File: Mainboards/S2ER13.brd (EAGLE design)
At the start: 43 x 72 mm, 52 parts, among them IC1 LD1117S33, IC2 CC1101RTK, IC3 STM32F051C8, Q1 IRLML9301, Q2 8M, X1 VCC, X2 CLK, X3 GND, X4 DIO, X5 RST, X6 NC

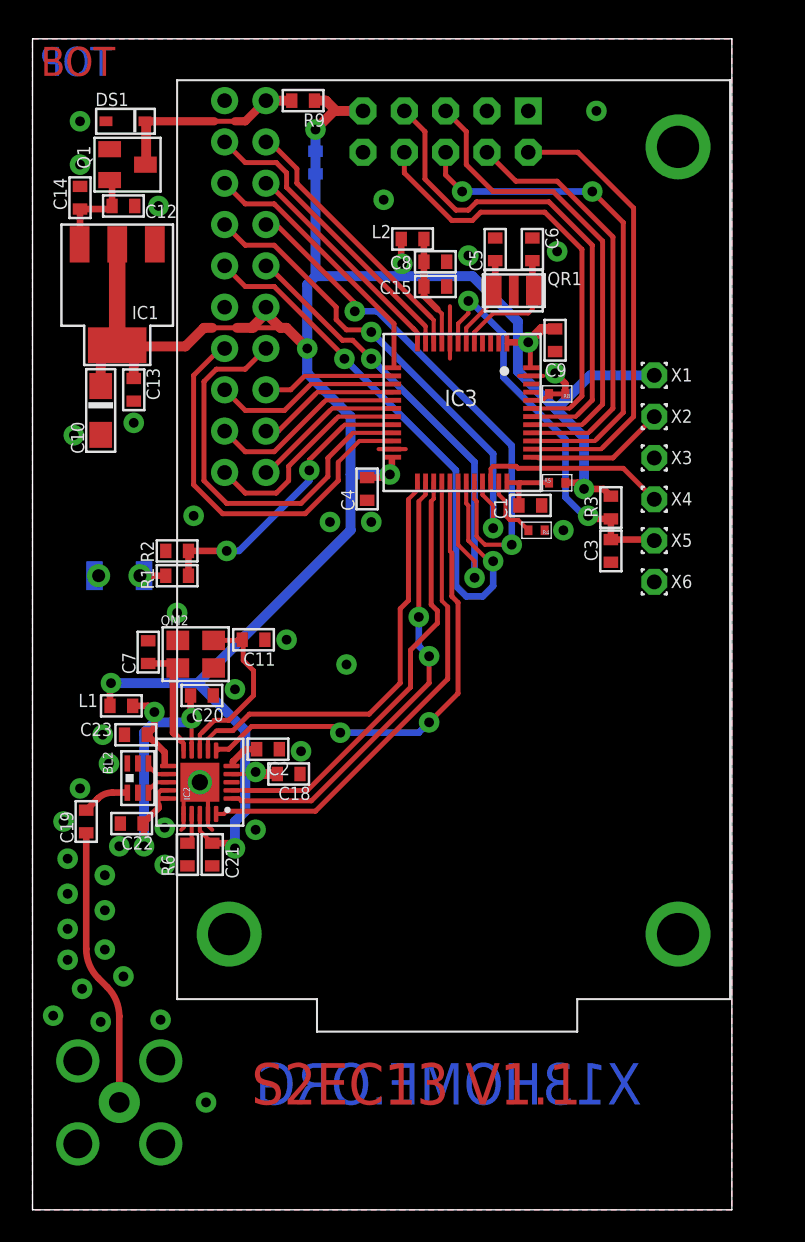
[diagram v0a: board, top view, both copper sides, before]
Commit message: Added prototypes
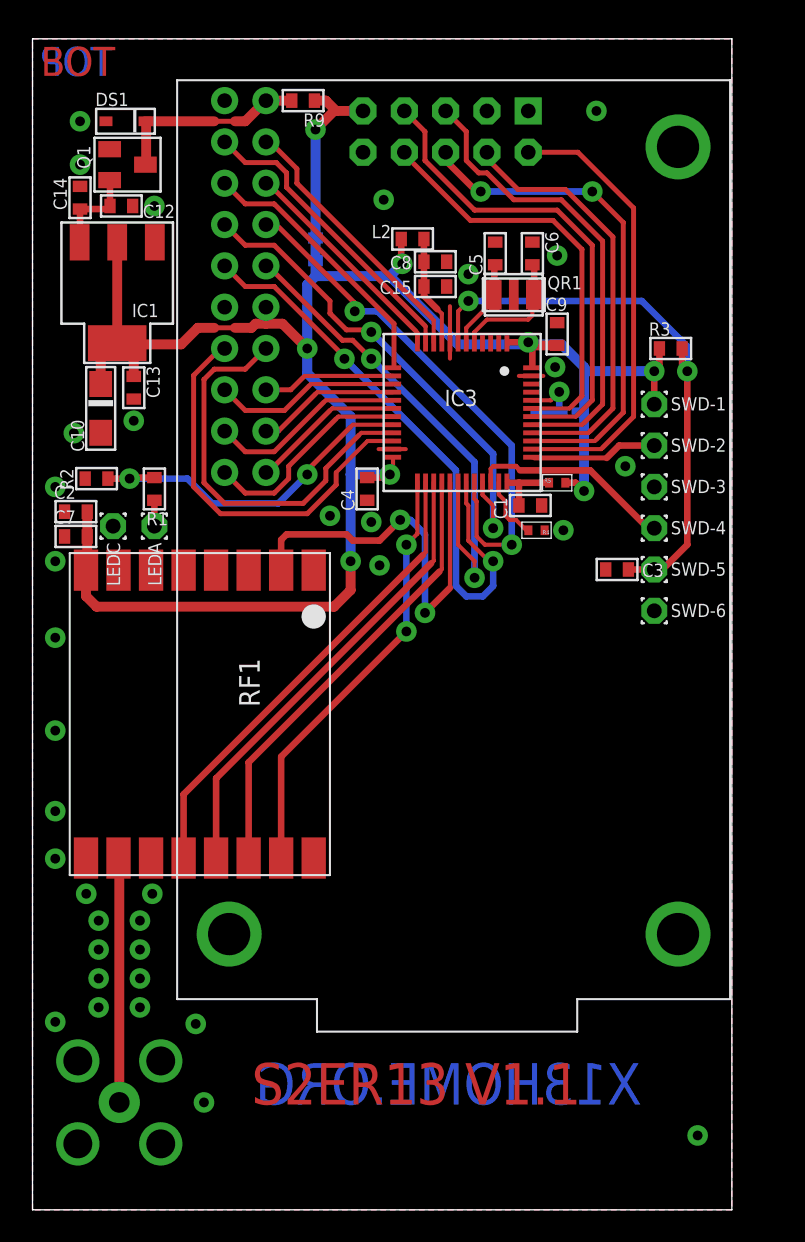
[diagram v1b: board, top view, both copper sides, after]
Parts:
- removed ANT: SMA-BU, Conn:BU-SMA-V
- removed BL2: 0896BM15A0001, RF:BL
- removed C11: 22p, RCL:0603
- removed C18, C20, C21, C22, C23: 100n, RCL:0603
- removed C19: 100p, RCL:0603
- removed IC2: CC1101RTK, RF:VQFN20
- removed L1: 10uH, RCL:0603
- removed LED1: OPT, Optic:T1-3/4
- removed LED2: OPT, Optic:1206
- removed QM2: 26M, QUARTZ:SMD_4P_3.2X2.5
- removed R6: 56k, RCL:0603
- removed R8: 0R, RCL:0402
- removed X1: VCC, Conn:T1.6/0.9
- removed X2: CLK, Conn:T1.6/0.9
- removed X4: DIO, Conn:T1.6/0.9
- removed X5: RST, Conn:T1.6/0.9
- removed X6: NC, Conn:T1.6/0.9
- added BR1: BR, Conn:BR
- added LEDA: LEDA, Conn:T1.6/0.9
- added LEDC, SWD-3: GND, Conn:T1.6/0.9
- added RF1: RFM69W, RF:RFM69
- added SWD-1: VCC, Conn:T1.6/0.9
- added SWD-2: CLK, Conn:T1.6/0.9
- added SWD-4: DIO, Conn:T1.6/0.9
- added SWD-5: /RST, Conn:T1.6/0.9
- added SWD-6: NC, Conn:T1.6/0.9
- C2: value 100n -> 1u
- C7: value 22p -> 100n
- X3: value GND -> SMA-BU; device Conn:T1.6/0.9 -> Conn:BU-SMA-V
- moved X3 51.5 mm to (5.33, 6.60), flipped to the bottom
- moved C2 18.8 mm to (2.67, 42.9), turned to 0 degrees
- moved R3 10.4 mm to (39.2, 53.0), turned to 0 degrees
- moved C7 8.39 mm to (2.67, 41.4), turned to 0 degrees
- moved R2 6.66 mm to (3.94, 45.0)
- moved R1 5.51 mm to (7.49, 44.3), turned to 90 degrees
- moved R7 5.33 mm to (17.4, 59.1)
- moved C3 1.20 mm to (35.9, 39.4), turned to 180 degrees
- moved C9 0.40 mm to (32.3, 53.8), turned to 270 degrees
- moved C5 0.25 mm to (28.4, 58.8)
- moved C6 0.25 mm to (30.7, 58.8)
- moved Q2 0.25 mm to (29.6, 56.3)
- moved QR1 0.25 mm to (29.6, 56.3)
- moved C10 0.13 mm to (4.19, 49.3)
- moved C13 0.13 mm to (6.22, 50.5)
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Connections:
- removed net BOOT0: IC3.44, R8.2
- removed net N$11: C11.2, IC2.-8, QM2.3
- removed net N$12: C7.1, IC2.-10, QM2.1
- removed net N$13: BL2.1, C19.1
- removed net N$14: ANT.1, C19.2
- removed net N$6: IC2.-17, R6.2
- removed net N$7: C2.2, IC2.-5
- removed net N$8: BL2.3, IC2.-13
- removed net N$9: BL2.4, IC2.-12
- removed net VDD: C20.2, C22.2, C23.2, IC2.-11, IC2.-14, IC2.-15, IC2.-9, L1.1
- new net BOOT: BR1.M, IC3.44
- new net N$5: RF1.-10, X3.1
- net +3V3: now also BR1.R, C2.2, C7.2, RF1.-8, SWD-1.1; no longer C18.2, C21.2, IC2.-18, IC2.-4, L1.2, X1.1
- net GND: now also BR1.L, C7.1, LEDC.1, RF1.-11, RF1.-9, SWD-3.1, X3.2, X3.3, X3.4, X3.5; no longer ANT.2, ANT.3, ANT.4, ANT.5, BL2.2, BL2.5, BL2.6, C11.1, C18.1, C20.1, C21.1, C22.1, C23.1, C7.2, IC2.-16, IC2.-19, IC2.P, LED1.C, LED2.2, QM2.2, QM2.4, R6.1, R8.1, X3.1
- net N$1: now also LEDA.1; no longer LED1.A, LED2.1
- net RST: now also SWD-5.1; no longer X5.1
- net R_IRQ: now also RF1.-2; no longer IC2.-6
- net R_MISO: now also RF1.-13; no longer IC2.-2
- net R_MOSI: now also RF1.-14; no longer IC2.-20
- net R_NSS: now also RF1.-15; no longer IC2.-7
- net R_SCK: now also RF1.-12; no longer IC2.-1
- net SWCLK: now also SWD-2.1; no longer X2.1
- net SWDIO: now also SWD-4.1; no longer X4.1
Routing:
- net VDD: track 24.9 -> 0.00 mm, vias 3 -> 0
- net N$14: track 17.1 -> 0.00 mm
- net +3V3: track 145.7 -> 131.1 mm, vias 9 -> 8
- net N$5: track 1.02 -> 15.0 mm
- net N$11: track 10.8 -> 0.00 mm
- net RST: track 24.8 -> 35.5 mm
- net N$12: track 7.40 -> 0.00 mm
- net GND: track 13.0 -> 6.37 mm, vias 41 -> 35
- net R_IRQ: track 29.9 -> 25.4 mm
- net LED: track 18.1 -> 21.9 mm
- net BOOT: track 0.00 -> 3.20 mm, vias 0 -> 1
- net N$13: track 2.89 -> 0.00 mm
- net N$7: track 2.08 -> 0.00 mm
- net R_MOSI: track 30.0 -> 28.1 mm
- net N$9: track 1.57 -> 0.00 mm
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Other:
- board text added: "S2ER13 V1.1"
- board text removed: "S2EC13 V1.1"

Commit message: S2ER13 Proto
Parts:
- removed BR1: BR, Conn:BR
- removed LEDA: LEDA, Conn:T1.6/0.9
- removed LEDC, SWD-3: GND, Conn:T1.6/0.9
- removed SWD-1: VCC, Conn:T1.6/0.9
- removed SWD-2: CLK, Conn:T1.6/0.9
- removed SWD-4: DIO, Conn:T1.6/0.9
- removed SWD-5: /RST, Conn:T1.6/0.9
- removed SWD-6: NC, Conn:T1.6/0.9
- added ANT: SMA-BU, Conn:BU-SMA-V
- added L1: 10uH, RCL:0603
- added LED1: OPT, Optic:T1-3/4
- added LED2: OPT, Optic:1206
- added R8: 10k, RCL:0603
- added X1: VCC, Conn:T1.6/0.9
- added X2: CLK, Conn:T1.6/0.9
- added X4: DIO, Conn:T1.6/0.9
- added X5: RST, Conn:T1.6/0.9
- added X6: NC, Conn:T1.6/0.9
- added X7: BOOT0, Conn:T1.6/0.9
- C2: value 1u -> 100n
- C7: value 100n -> 1u
- R4, R5: device RCL:0402 -> RCL:0603
- RF1: value RFM69W -> RFM69CW; device RF:RFM69 -> RF:RFM69CW
- X3: value SMA-BU -> GND; device Conn:BU-SMA-V -> Conn:T1.6/0.9
- moved X3 51.6 mm to (38.4, 46.2), flipped to the top
- moved C7 27.4 mm to (24.1, 24.4), turned to 270 degrees
- moved C2 27.0 mm to (22.4, 24.4), turned to 90 degrees
- moved R3 9.80 mm to (36.1, 43.7), turned to 270 degrees
- moved R2 6.25 mm to (8.89, 41.1)
- moved R7 5.33 mm to (17.4, 64.4)
- moved R1 4.90 mm to (8.89, 39.6), turned to 0 degrees
- moved RF1 2.16 mm to (11.9, 29.1), turned to 0 degrees
- moved C3 1.66 mm to (36.1, 41.0), turned to 270 degrees
- moved C1 1.49 mm to (32.0, 42.8), turned to 270 degrees
- moved R4 1.09 mm to (30.6, 42.8), turned to 90 degrees
- moved C9 0.40 mm to (32.1, 53.5), turned to 90 degrees
- moved R5 0.38 mm to (32.6, 44.7)
- moved C5 0.25 mm to (28.4, 59.1)
- moved C6 0.25 mm to (30.7, 59.1)
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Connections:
- removed net BOOT: BR1.M, IC3.44
- new net BOOT0: IC3.44, R8.2, X7.1
- new net VDDR: C2.2, C7.1, L1.1, RF1.VDD
- net +3V3: now also L1.2, X1.1; no longer BR1.R, C2.2, C7.2, RF1.-8, SWD-1.1
- net GND: now also ANT.2, ANT.3, ANT.4, ANT.5, C7.2, LED1.C, LED2.2, R8.1, RF1.GND@14, RF1.GND@3, X3.1; no longer BR1.L, C7.1, LEDC.1, RF1.-11, RF1.-9, SWD-3.1, X3.2, X3.3, X3.4, X3.5
- net N$1: now also LED1.A, LED2.1; no longer LEDA.1
- net N$5: now also ANT.1, RF1.ANA; no longer RF1.-10, X3.1
- net RST: now also X5.1; no longer SWD-5.1
- net R_IRQ: now also RF1.DIO0; no longer RF1.-2
- net R_MISO: now also RF1.MISO; no longer RF1.-13
- net R_MOSI: now also RF1.MOSI; no longer RF1.-14
- net R_NSS: now also RF1.NSS; no longer RF1.-15
- net R_SCK: now also RF1.SCK; no longer RF1.-12
- net SWCLK: now also X2.1; no longer SWD-2.1
- net SWDIO: now also X4.1; no longer SWD-4.1
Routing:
- net BOOT0: track 0.00 -> 15.9 mm, vias 0 -> 1
- net R_SCK: track 29.3 -> 14.5 mm
- net R_NSS: track 26.6 -> 12.3 mm, vias 2 -> 0
- net R_MOSI: track 28.1 -> 17.0 mm
- net RST: track 35.5 -> 24.5 mm
- net N$5: track 15.0 -> 23.9 mm
- net VDDR: track 0.00 -> 6.25 mm
- net +3V3: track 131.1 -> 126.0 mm, vias 8 -> 7
- net LED: track 21.9 -> 18.0 mm
- net R_IRQ: track 25.4 -> 28.8 mm
- net BOOT: track 3.20 -> 0.00 mm, vias 1 -> 0
- net R_MISO: track 28.7 -> 25.8 mm, vias 0 -> 2
- net PA9: track 31.3 -> 28.7 mm
- net PA10: track 36.8 -> 34.4 mm
- net L_RST/RX1: track 25.9 -> 27.2 mm
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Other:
- board text added: "+"
- board text added: "B"
- board text added: "G"
- board text added: "R"
